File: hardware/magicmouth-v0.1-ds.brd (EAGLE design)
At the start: 100 x 80 mm, 39 parts, among them IC1 LM386N, IC2 ATMEGA168-20P, Q1 16Mhz, U1 ARDUINOR3-NOIOREF-NOTEXT

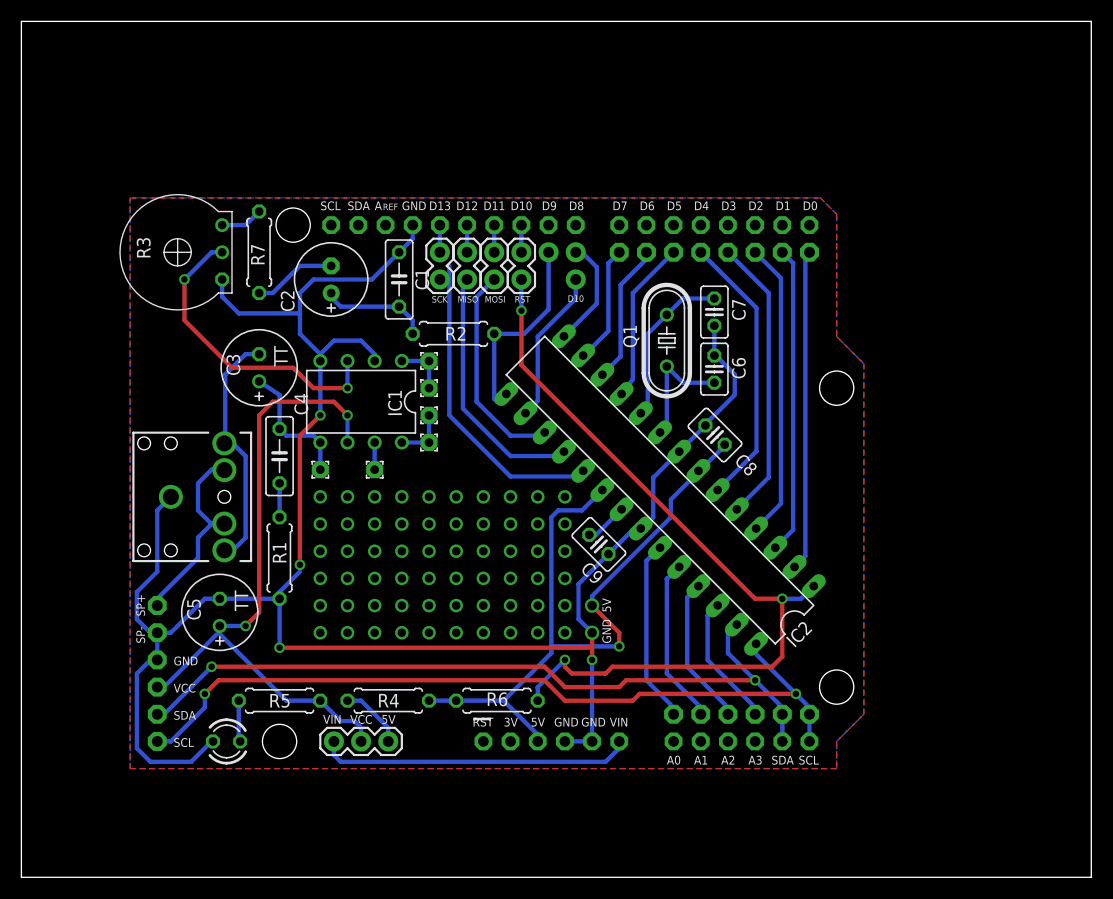
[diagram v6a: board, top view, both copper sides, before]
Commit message: adjusted placement to avoid through holes directly above Arduino USB port
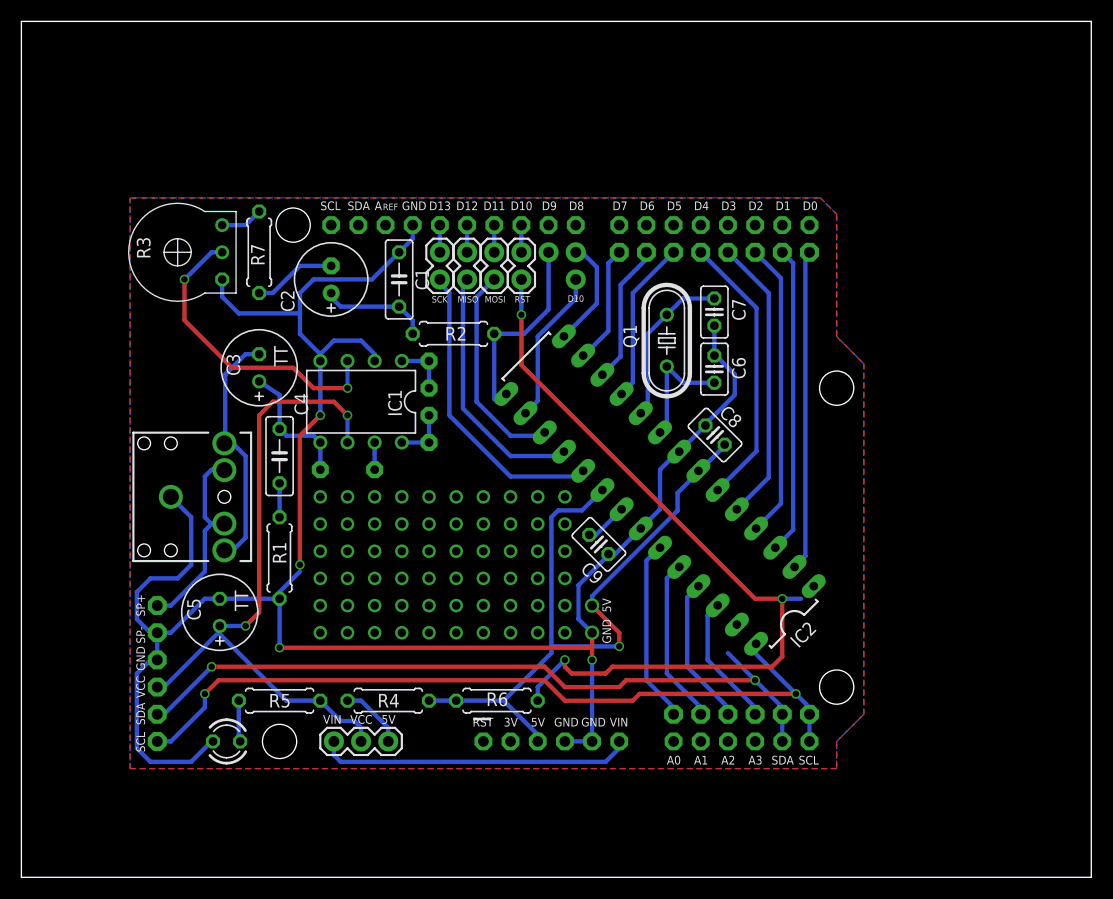
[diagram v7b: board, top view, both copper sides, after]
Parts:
- IC2: value ATMEGA168-20P -> ATMEGA328P_PDIP; device adafruit:DIL28-3 -> SparkFun-DigitalIC:DIL28-3
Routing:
- net GND: track 191.9 -> 194.8 mm
- net SDA: track 72.2 -> 70.3 mm
- net SS: track 77.0 -> 75.3 mm
- net SIGNAL: track 19.0 -> 18.0 mm
- net SP+: track 19.4 -> 20.4 mm
- net SCK: track 29.1 -> 28.2 mm
- net MISO: track 23.7 -> 23.1 mm
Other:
- board text added: "http://is.gd/magicmouth"
- board text removed: "http://tinyurl.com/magicmouth"
